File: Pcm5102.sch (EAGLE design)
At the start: 24 parts

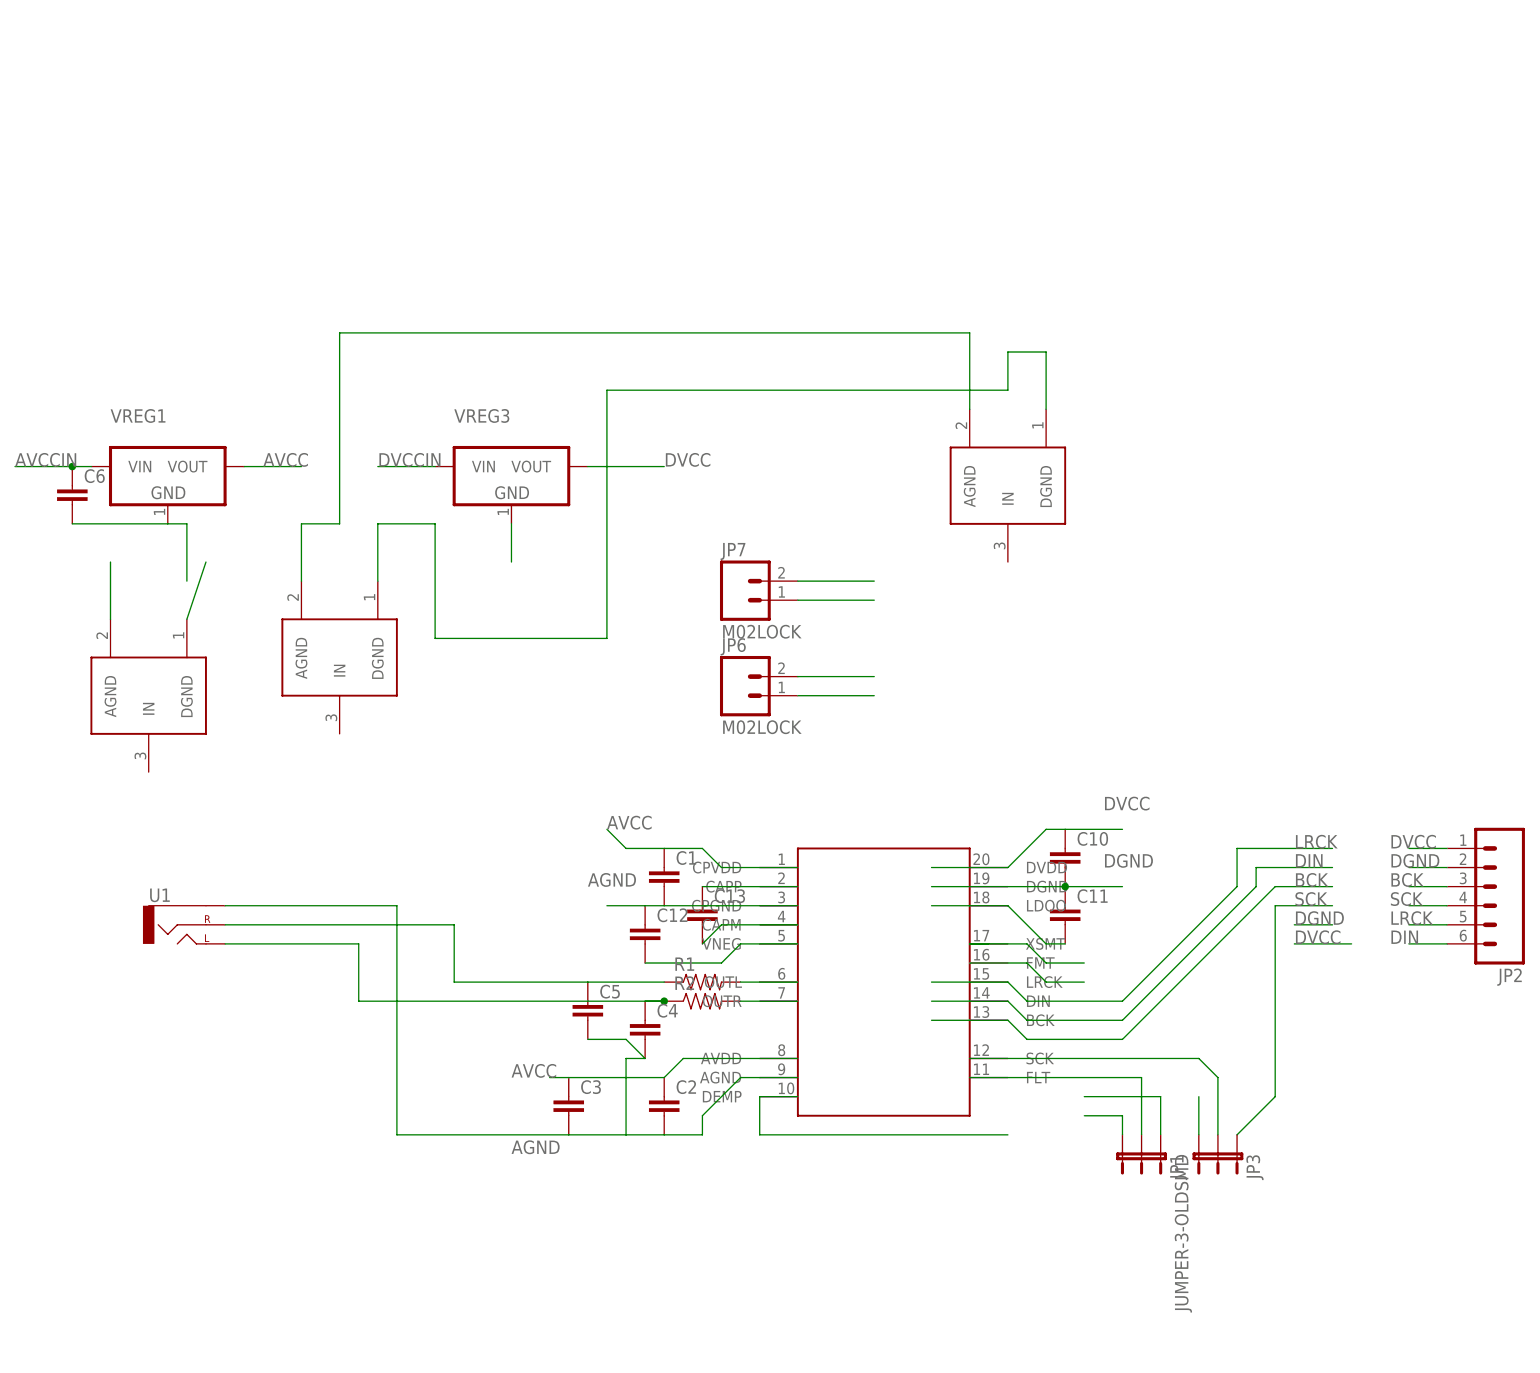
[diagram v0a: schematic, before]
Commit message: V1.2
Change LDO from LM1117 to LP5907 (Ultra Low noise)
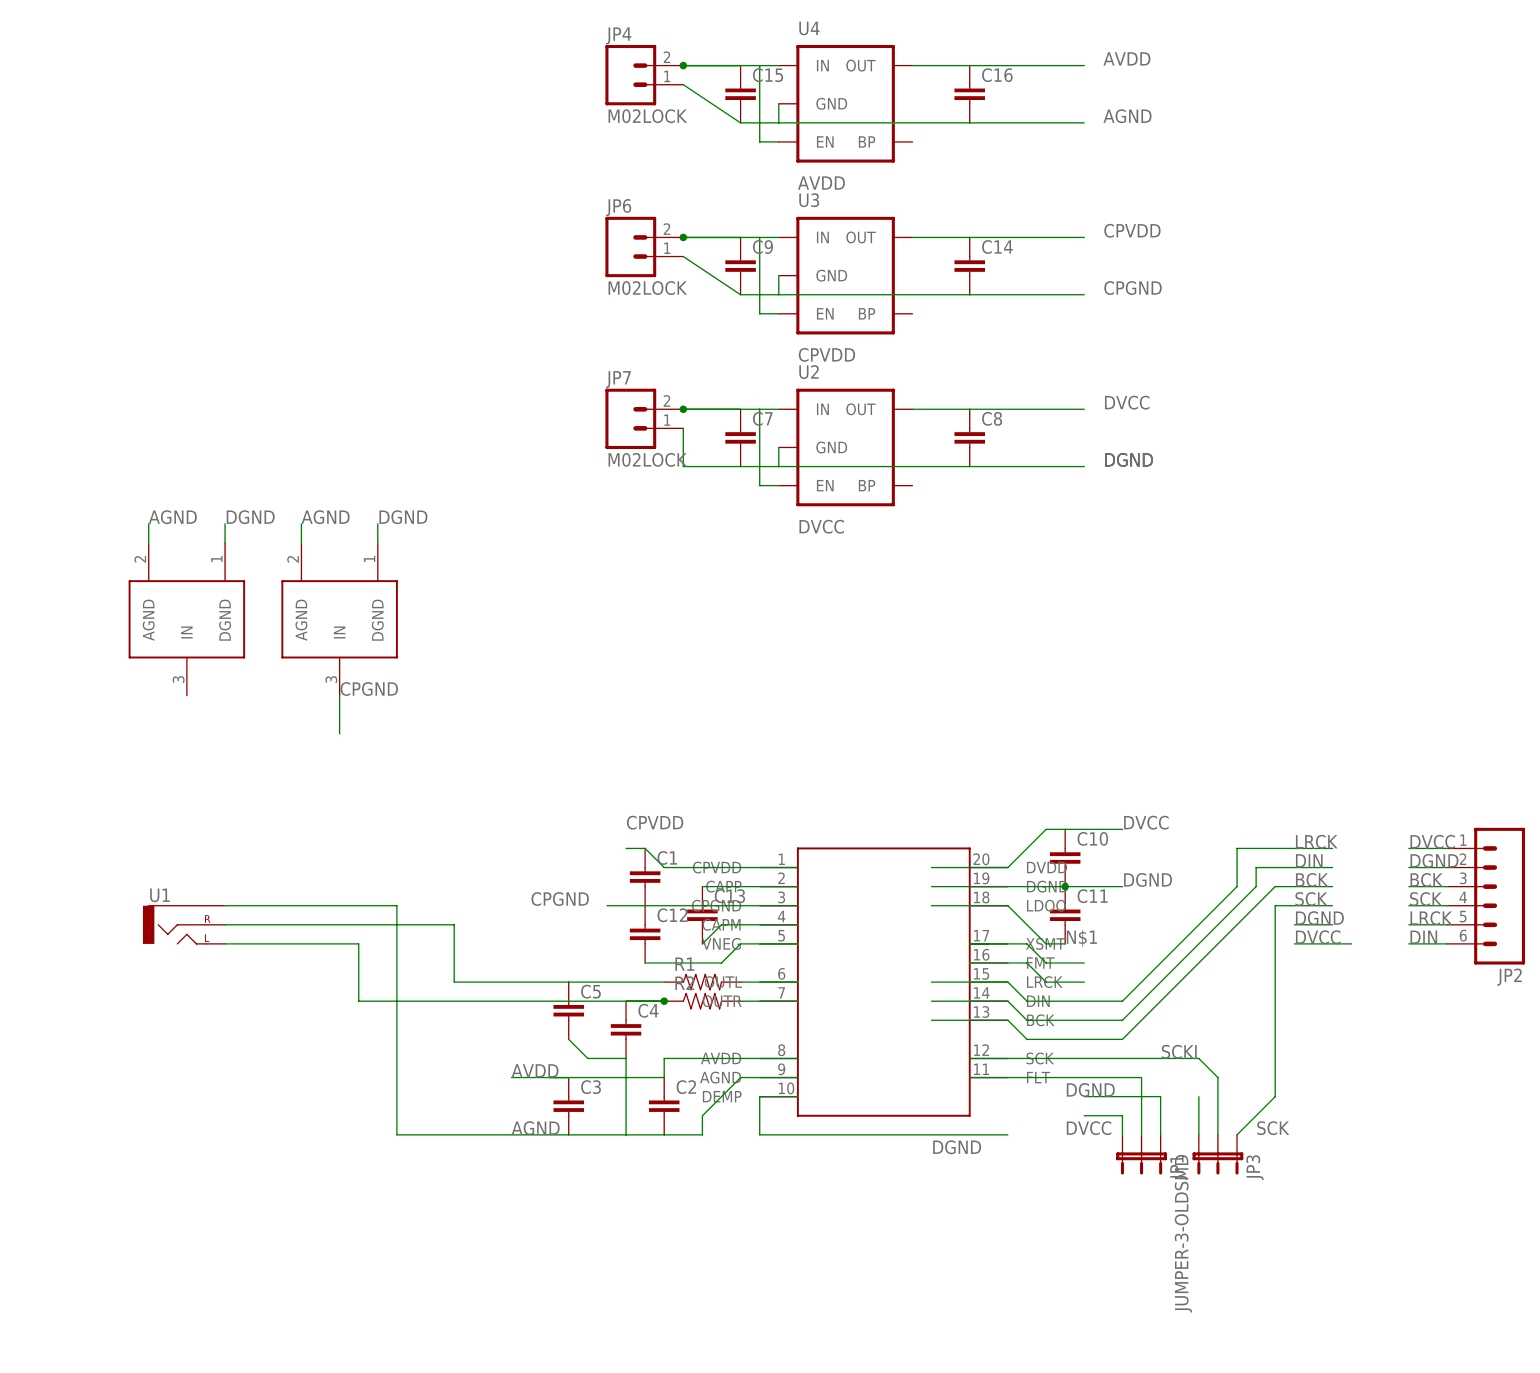
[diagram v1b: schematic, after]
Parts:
- removed C6: (no value), SparkFun-Capacitors:CAP0805
- removed U$4: GND_CONNECT, SparkFun-Passives:GND_CONNECT
- removed VREG1, VREG3: (no value), dp_devices:VREG_3PINS-SOT-223
- added C14, C15, C16, C7, C8, C9: (no value), SparkFun-Capacitors:CAP0805
- added JP4: M02LOCK, SparkFun-Connectors:M02LOCK
- added U2: DVCC, SparkFun-PowerIC:V_REG_LDOSMD
- added U3: CPVDD, SparkFun-PowerIC:V_REG_LDOSMD
- added U4: AVDD, SparkFun-PowerIC:V_REG_LDOSMD
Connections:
- removed net AVCC: C1.1, C2.1, C3.1, U$1.AVDD, U$1.CPVDD, VREG1.VOUT
- removed net AVCCIN: C6.1, JP6.2, VREG1.VIN
- removed net DVCCIN: JP7.2, VREG3.VIN
- removed net DVDD: U$1.XSMT
- new net AVDD: C16.1, C2.1, C3.1, U$1.AVDD, U4.OUT
- new net CPGND: C1.2, C12.1, C14.2, C9.2, JP6.1, U$1.CPGND, U$2.IN, U3.GND
- new net CPVDD: C1.1, C14.1, U$1.CPVDD, U3.OUT
- new net N$10: C15.1, JP4.2, U4.EN, U4.IN
- new net N$15: C9.1, JP6.2, U3.EN, U3.IN
- new net N$16: C7.1, JP7.2, U2.EN, U2.IN
- net AGND: now also C15.2, C16.2, JP4.1, U4.GND; no longer C1.2, C12.1, C6.2, JP6.1, U$1.CPGND, U$4.AGND, VREG1.GND
- net DGND: now also C7.2, C8.2, U2.GND; no longer U$4.DGND, VREG3.GND
- net DVCC: now also C8.1, U$1.XSMT, U2.OUT; no longer VREG3.VOUT
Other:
- moved on the sheet: C1, C4, C5, JP6, JP7
